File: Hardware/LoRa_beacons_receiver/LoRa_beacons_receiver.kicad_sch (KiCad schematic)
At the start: 45 parts, among them J1 Conn_Coaxial, J2 USB_C_Receptacle_USB2.0_16P, J3 I2C_Display, J4 ST-Link, J5 1PPS_out, J6 Conn_02x09_Counter_Clockwise, SW1 RST_button, SW2 BOOT_button, U1 STM32WLE5JC, U2 CP2102N-Axx-xQFN28, U3 AP2112K-3.3, U4 74LVC1G175

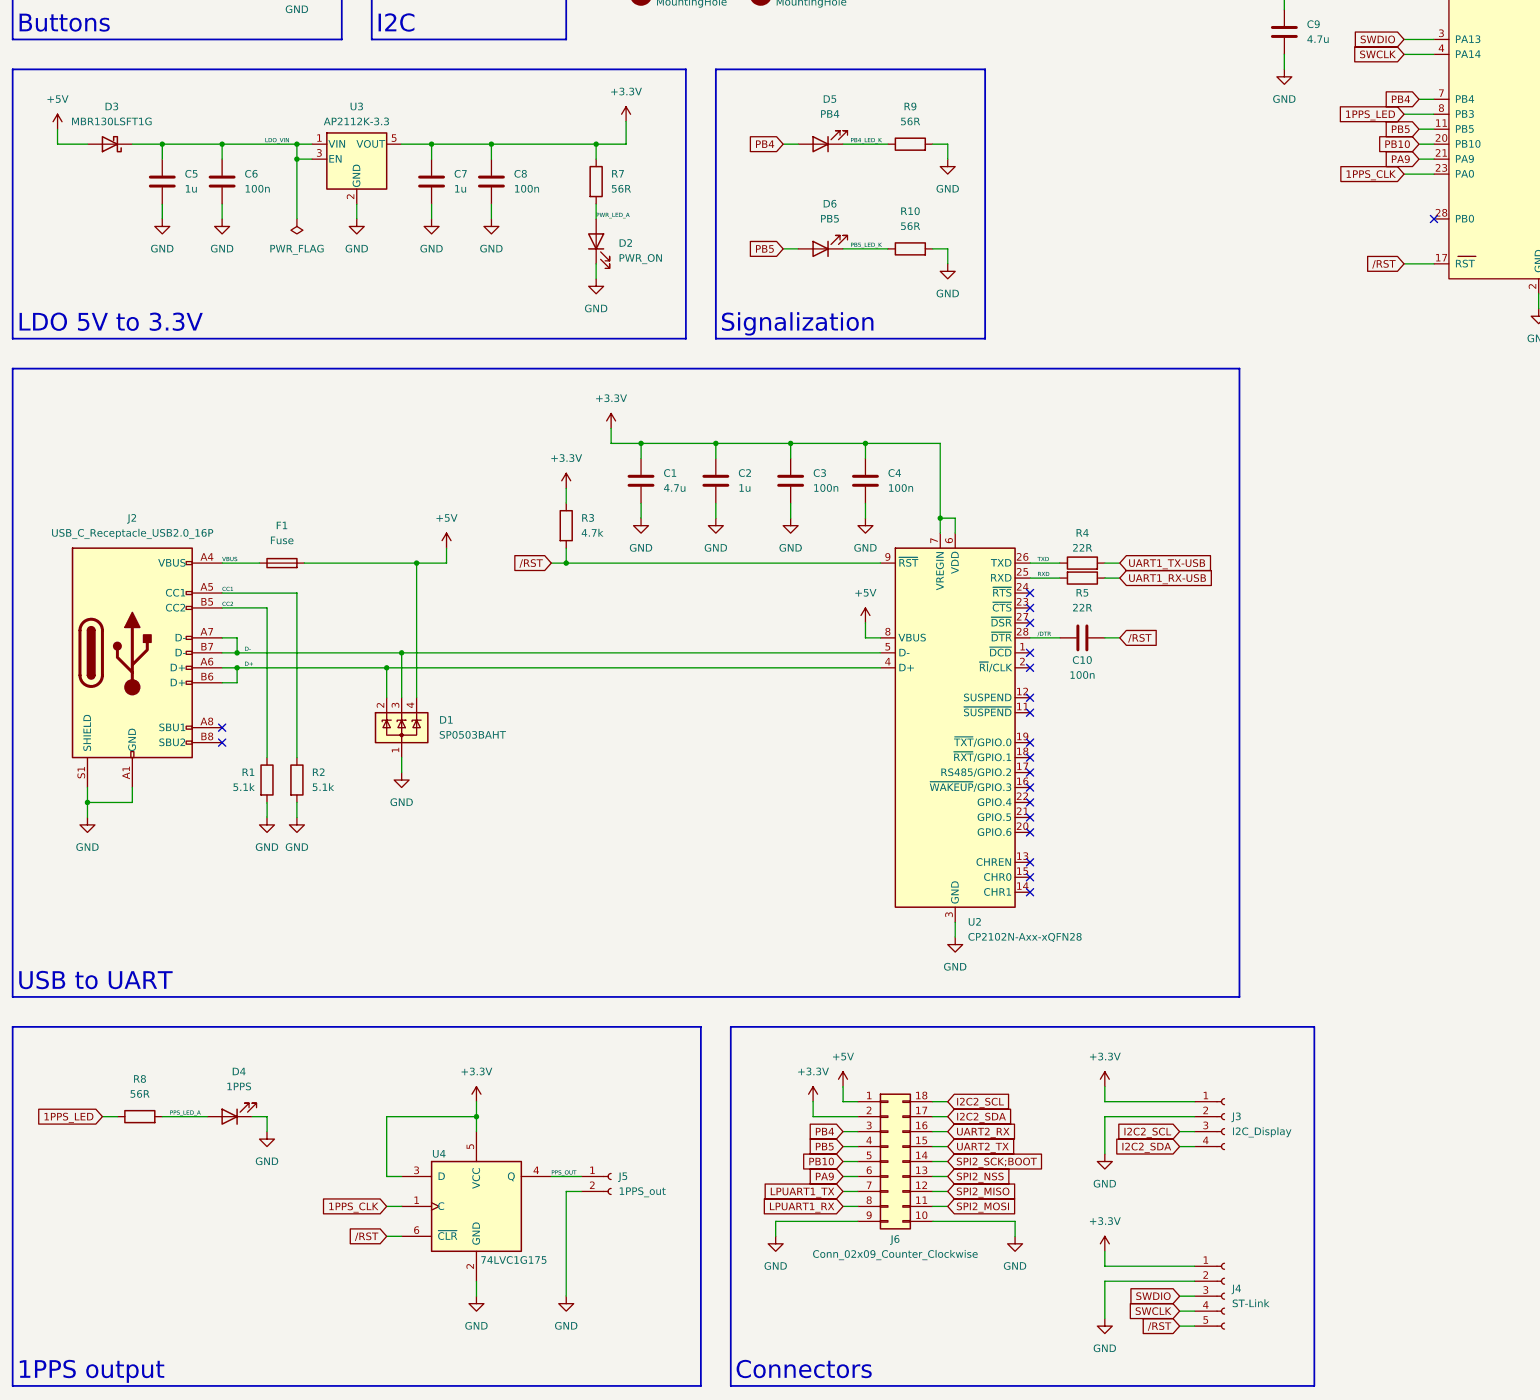
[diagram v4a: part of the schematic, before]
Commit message: Minor schematic changes
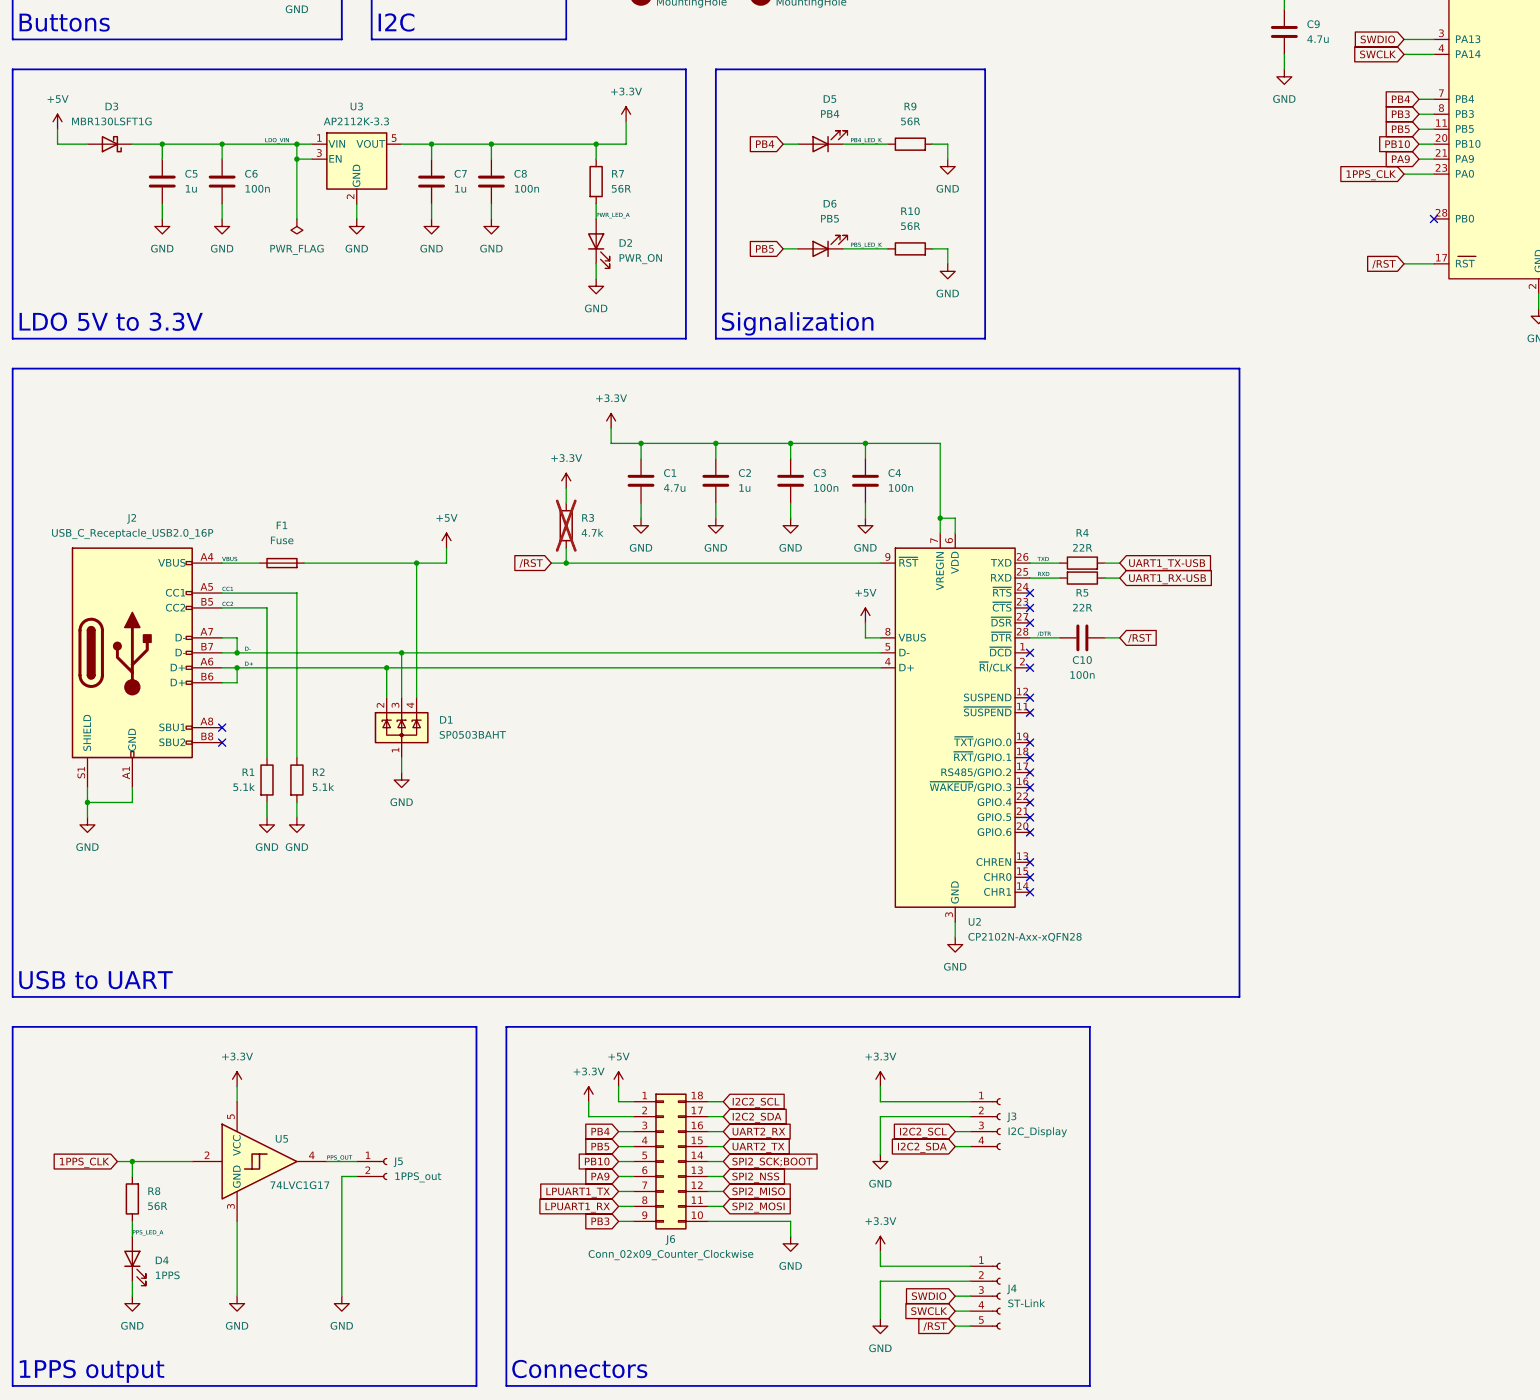
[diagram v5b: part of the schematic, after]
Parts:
- removed U4: 74LVC1G175, Package_TO_SOT_SMD:SOT-23-6_Handsoldering, symbol 74xGxx:74LVC1G175
- added U5: 74LVC1G17, Package_TO_SOT_SMD:SOT-23-5_HandSoldering, symbol 74xGxx:74LVC1G17
- D3: footprint Diode_SMD_l:SOD-123FL -> Diode_SMD_l:SOD-123FL_l
- R3: now not fitted
- U1: footprint STM32_module_l:STM32WLE5JC -> STM32_module_l:STM32WLE5JC_l
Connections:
- net +3.3V: now also U5.5 (VCC)
- net 1PPS_CLK: now also R8.2, U5.2
- net GND: now also U5.3 (GND); no longer J6.9 (Pin_9)
- net PPS_LED_A: now also R8.1; no longer R8.2
- net PPS_OUT: now also U5.4
- net 1PPS_LED renamed PB3
- net PB3: now also J6.9 (Pin_9); no longer R8.1
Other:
- moved on the sheet: D4, J3, J4, J5, J6, R8

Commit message: Minor schematic changes; PCB WIP
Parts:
- removed C4: 100n, Capacitor_SMD:C_0805_2012Metric_Pad1.18x1.45mm_HandSolder, symbol Device:C
- C1: value 4.7u -> 100n
- R3: now left out of the parts list
- U1: value STM32WLE5JC -> Wio-E5
- renumbered C9 to C4
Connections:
- net +3.3V: now also C1.1; no longer C1.2
- net GND: now also C1.2; no longer C1.1
- net D+ renamed USB_D_P
- net D- renamed USB_D_N
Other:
- moved on the sheet: C10, C2, C3, C4, D4, J1, J5, R4, R5, R8, U1, U2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

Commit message: First version of completely routed PCB
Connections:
- net +3.3V: now also J6.1 (Pin_1); no longer J6.2 (Pin_2)
- net +5V: no longer J6.1 (Pin_1)
- net GND: now also J6.2 (Pin_2); no longer J6.10 (Pin_10)
- net I2C2_SCL: now also J6.3 (Pin_3); no longer J6.18 (Pin_18)
- net I2C2_SDA: now also J6.4 (Pin_4); no longer J6.17 (Pin_17)
- net LPUART1_RX: now also J6.9 (Pin_9); no longer J6.8 (Pin_8)
- net LPUART1_TX: now also J6.10 (Pin_10); no longer J6.7 (Pin_7)
- net PA9: now also J6.16 (Pin_16); no longer J6.6 (Pin_6)
- net PB10: now also J6.15 (Pin_15); no longer J6.5 (Pin_5)
- net PB3: now also J6.5 (Pin_5); no longer J6.9 (Pin_9)
- net PB4: now also J6.6 (Pin_6); no longer J6.3 (Pin_3)
- net PB5: now also J6.7 (Pin_7); no longer J6.4 (Pin_4)
- net SPI2_MISO: now also J6.11 (Pin_11); no longer J6.12 (Pin_12)
- net SPI2_MOSI: now also J6.12 (Pin_12); no longer J6.11 (Pin_11)
- net SPI2_NSS: now also J6.14 (Pin_14); no longer J6.13 (Pin_13)
- net SPI2_SCK;BOOT: now also J6.13 (Pin_13); no longer J6.14 (Pin_14)
- net UART2_RX: now also J6.17 (Pin_17); no longer J6.16 (Pin_16)
- net UART2_TX: now also J6.18 (Pin_18); no longer J6.15 (Pin_15)
- net PB0: now reaches U1.28 (PB0)
- net PB0: now also J6.8 (Pin_8)
- no-connect marks 20 -> 19
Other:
- moved on the sheet: C4, J1, J6, U1

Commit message: Minor changes
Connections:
- net +3.3V: now also J6.2 (Pin_2); no longer J6.1 (Pin_1)
- net GND: now also J6.8 (Pin_8); no longer J6.2 (Pin_2)
- net PB0: now also J6.1 (Pin_1); no longer J6.8 (Pin_8)
- net UART1_RX-USB renamed UART1_TX-USB_RX
- net UART1_TX-USB renamed UART1_RX-USB_TX
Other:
- moved on the sheet: C10, R4, R5, U2
